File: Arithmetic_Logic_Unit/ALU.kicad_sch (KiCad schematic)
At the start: 21 parts, among them U3 74LS86, U4 74LS86, U5 74LS283, U6 74LS283, U7 74LS245

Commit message: added flags
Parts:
- added U10: 74LS08, symbol 74xx:74LS08
- added U11: 74LS02, symbol 74xx:74LS02
- added U9: 74LS173, symbol 74xx:74LS173
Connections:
- net 5V: now also U10.14 (VCC), U11.14 (VCC), U9.16 (VCC)
- net GND: now also U10.12, U10.13, U10.7 (GND), U11.7 (GND), U9.1 (Oe1), U9.2 (Oe2), U9.8 (GND)
- net clock: now also U9.7 (Cp)
- net s0: now also U11.12
- net s1: now also U11.11
- net s2: now also U11.9
- net s3: now also U11.8
- net s4: now also U11.6
- net s5: now also U11.5
- net s6: now also U11.3
- net s7: now also U11.2
- net at U5.9 (C4): now also U9.14 (D0)
- new net: U10.4, U11.10
- new net: U10.5, U11.13
- new net: U10.10, U10.6
- new net: U10.1, U11.1
- new net: U10.2, U11.4
- new net: U10.3, U10.9
- new net: U10.8, U9.13 (D1)
- new net cf: U9.3 (Q0)
- new net clear: U9.15 (Mr)
- new net fi: U9.10 (E2), U9.9 (E1)
- new net zf: U9.4 (Q1)
- no-connect marks 0 -> 5

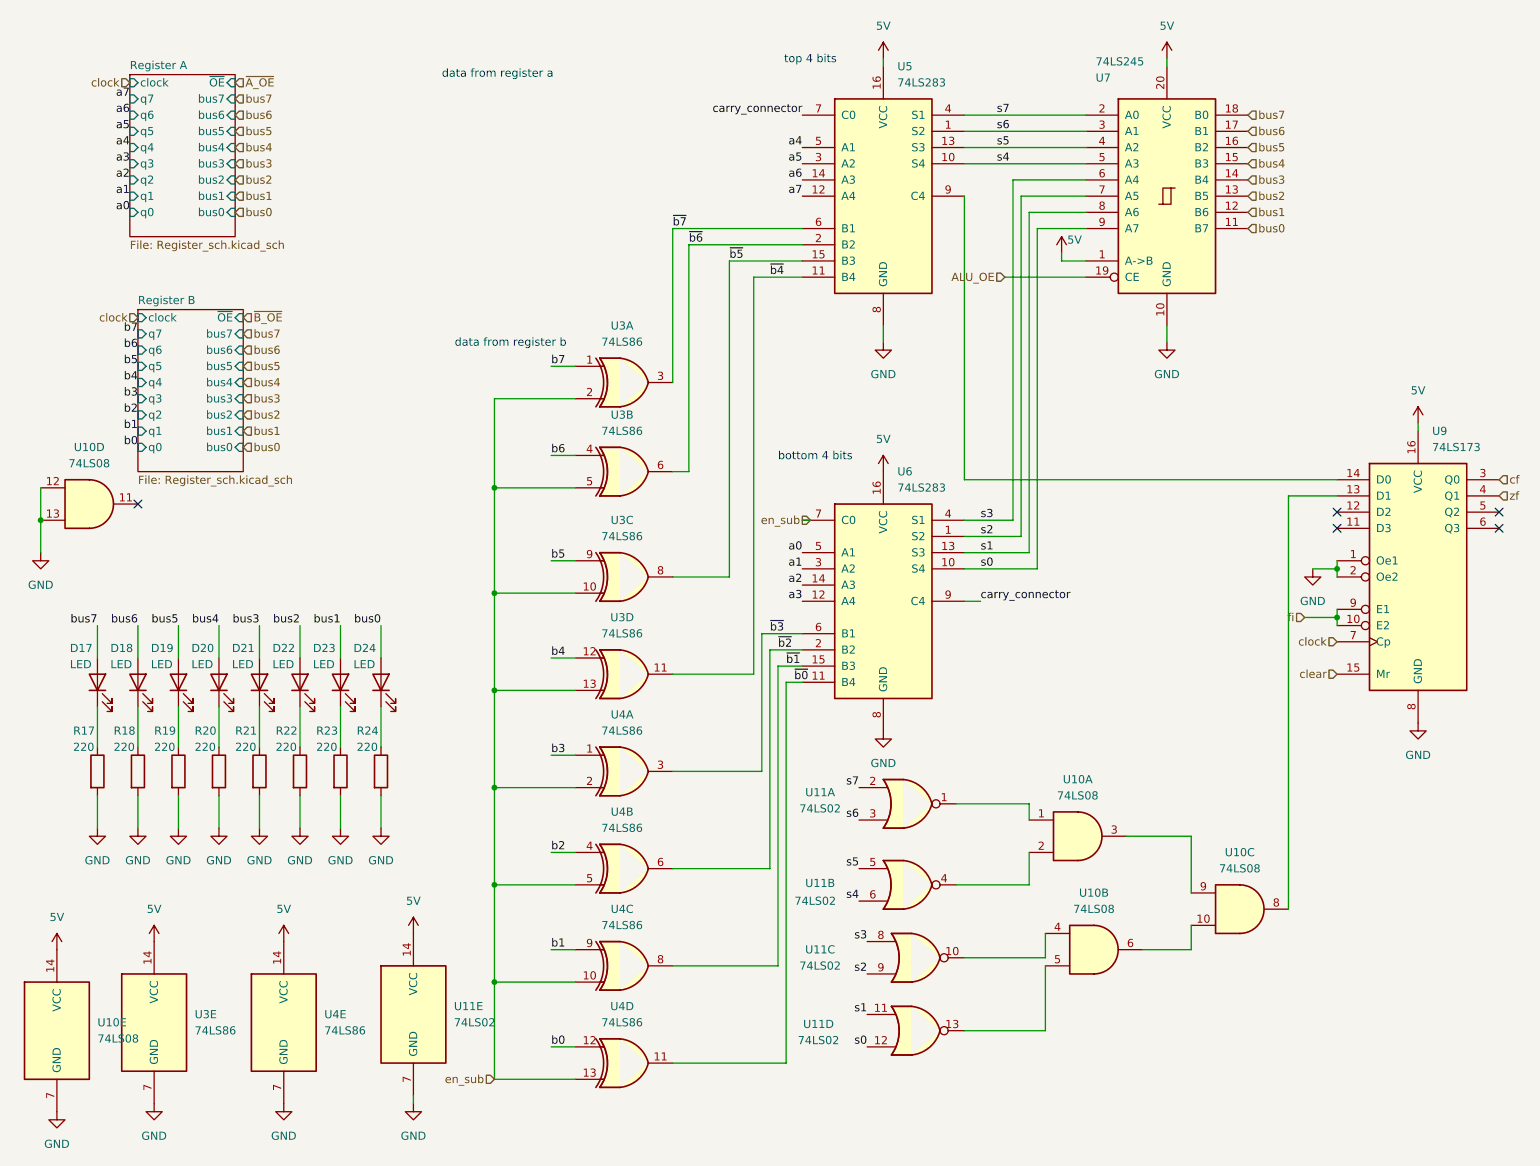
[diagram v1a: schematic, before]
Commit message: fixed incorrect footprint for sn54173
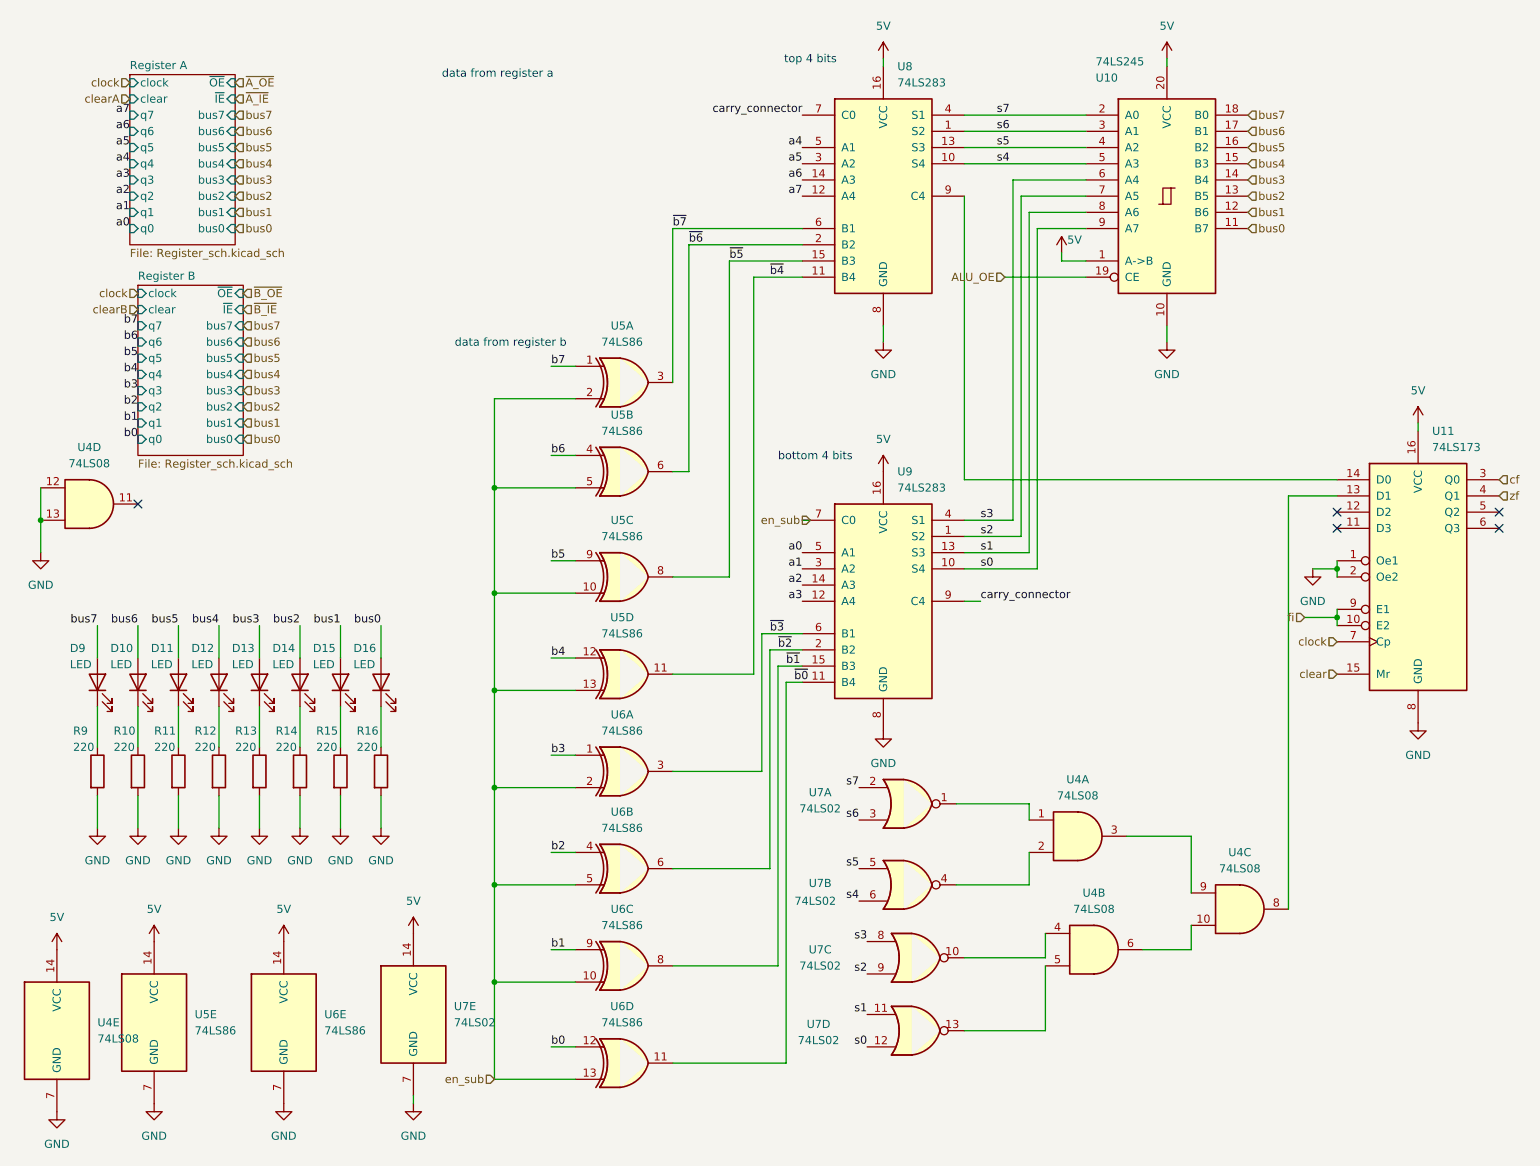
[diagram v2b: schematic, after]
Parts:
- renumbered D18 to D10, D19 to D11, D20 to D12, D21 to D13, D22 to D14, D23 to D15, D24 to D16, D17 to D9, R18 to R10, R19 to R11, R20 to R12, R21 to R13, R22 to R14, R23 to R15, R24 to R16, R17 to R9, U7 to U10, U9 to U11, U10 to U4, U3 to U5, U4 to U6, U11 to U7, U5 to U8, U6 to U9
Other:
- sheet Register A ports: added clear, ~{IE}; removed none
- sheet Register B ports: added clear, ~{IE}; removed none

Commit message: fixed wiring issues
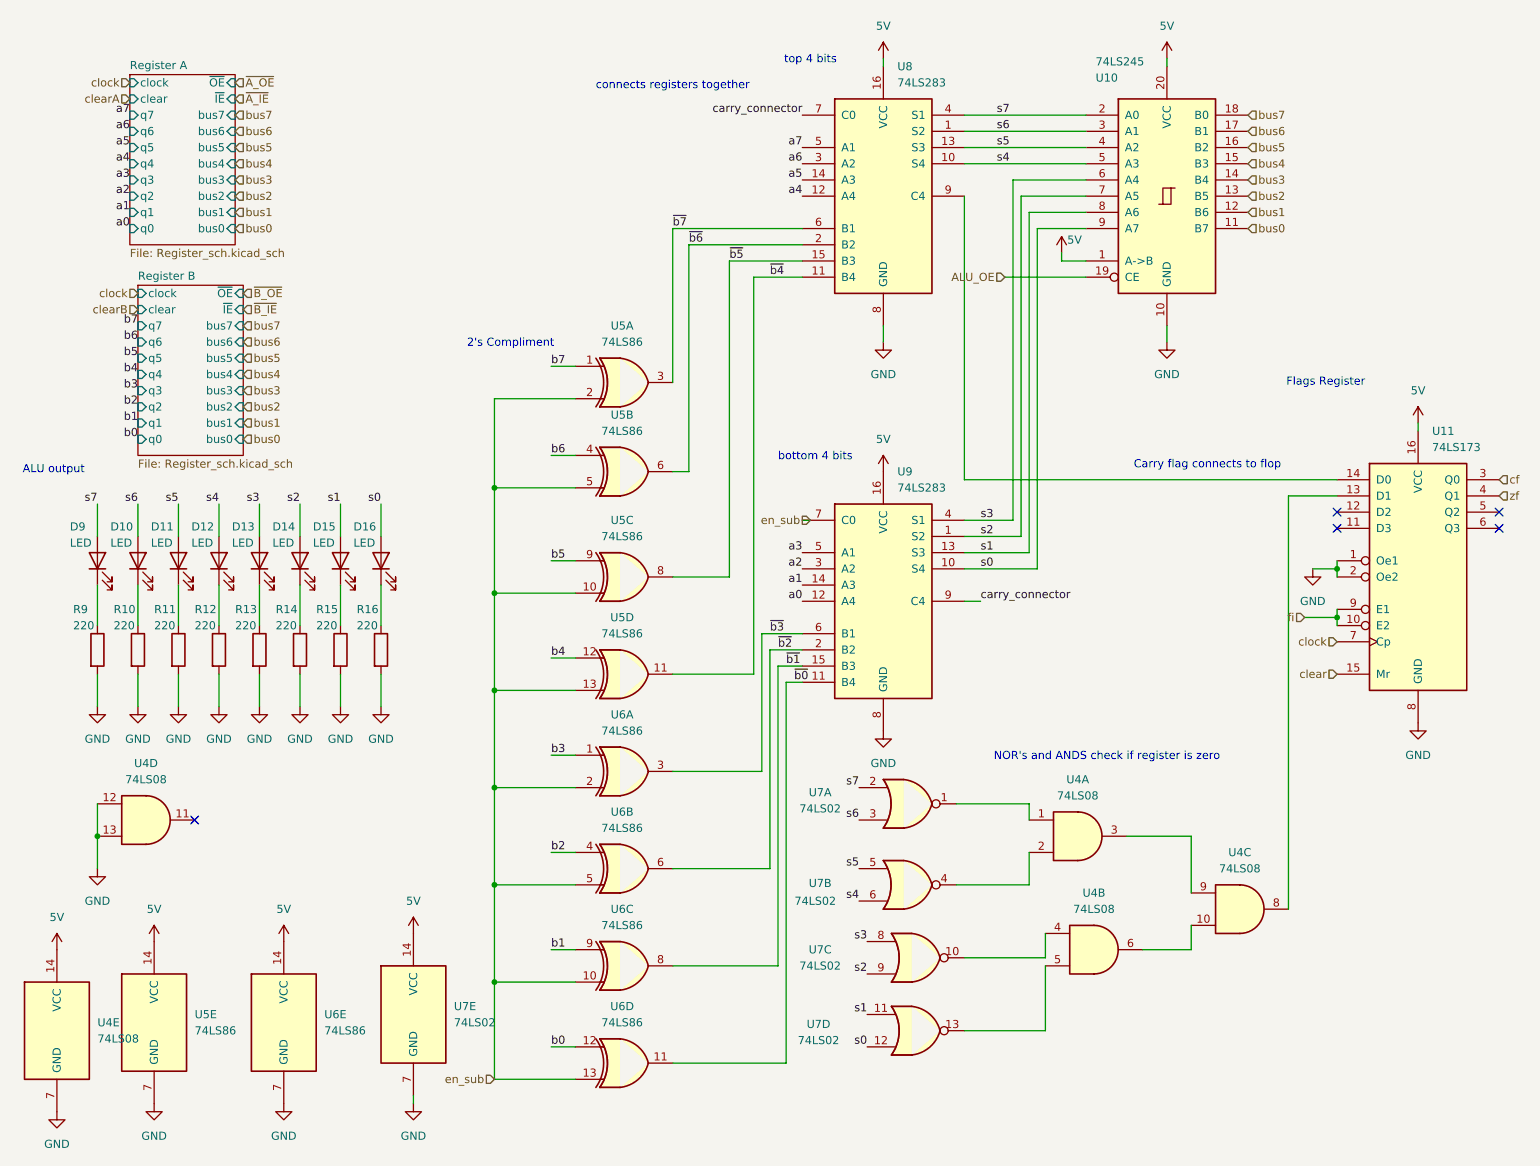
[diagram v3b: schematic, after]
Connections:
- net a0: now also U9.12 (A4); no longer U9.5 (A1)
- net a1: now also U9.14 (A3); no longer U9.3 (A2)
- net a2: now also U9.3 (A2); no longer U9.14 (A3)
- net a3: now also U9.5 (A1); no longer U9.12 (A4)
- net a4: now also U8.12 (A4); no longer U8.5 (A1)
- net a5: now also U8.14 (A3); no longer U8.3 (A2)
- net a6: now also U8.3 (A2); no longer U8.14 (A3)
- net a7: now also U8.5 (A1); no longer U8.12 (A4)
- net bus0: no longer D16.2 (A)
- net bus1: no longer D15.2 (A)
- net bus2: no longer D14.2 (A)
- net bus3: no longer D13.2 (A)
- net bus4: no longer D12.2 (A)
- net bus5: no longer D11.2 (A)
- net bus6: no longer D10.2 (A)
- net bus7: no longer D9.2 (A)
- net s0: now also D16.2 (A)
- net s1: now also D15.2 (A)
- net s2: now also D14.2 (A)
- net s3: now also D13.2 (A)
- net s4: now also D12.2 (A)
- net s5: now also D11.2 (A)
- net s6: now also D10.2 (A)
- net s7: now also D9.2 (A)
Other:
- note added: "2's Compliment"
- note added: "ALU output"
- note added: "Carry flag connects to flop"
- note added: "Flags Register"
- note added: "NOR's and ANDS check if register is zero"
- note added: "connects registers together"
- note removed: "data from register a"
- note removed: "data from register b"
- moved on the sheet: D10, D11, D12, D13, D14, D15, D16, D9, R10, R11, R12, R13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

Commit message: added bypass capacitors
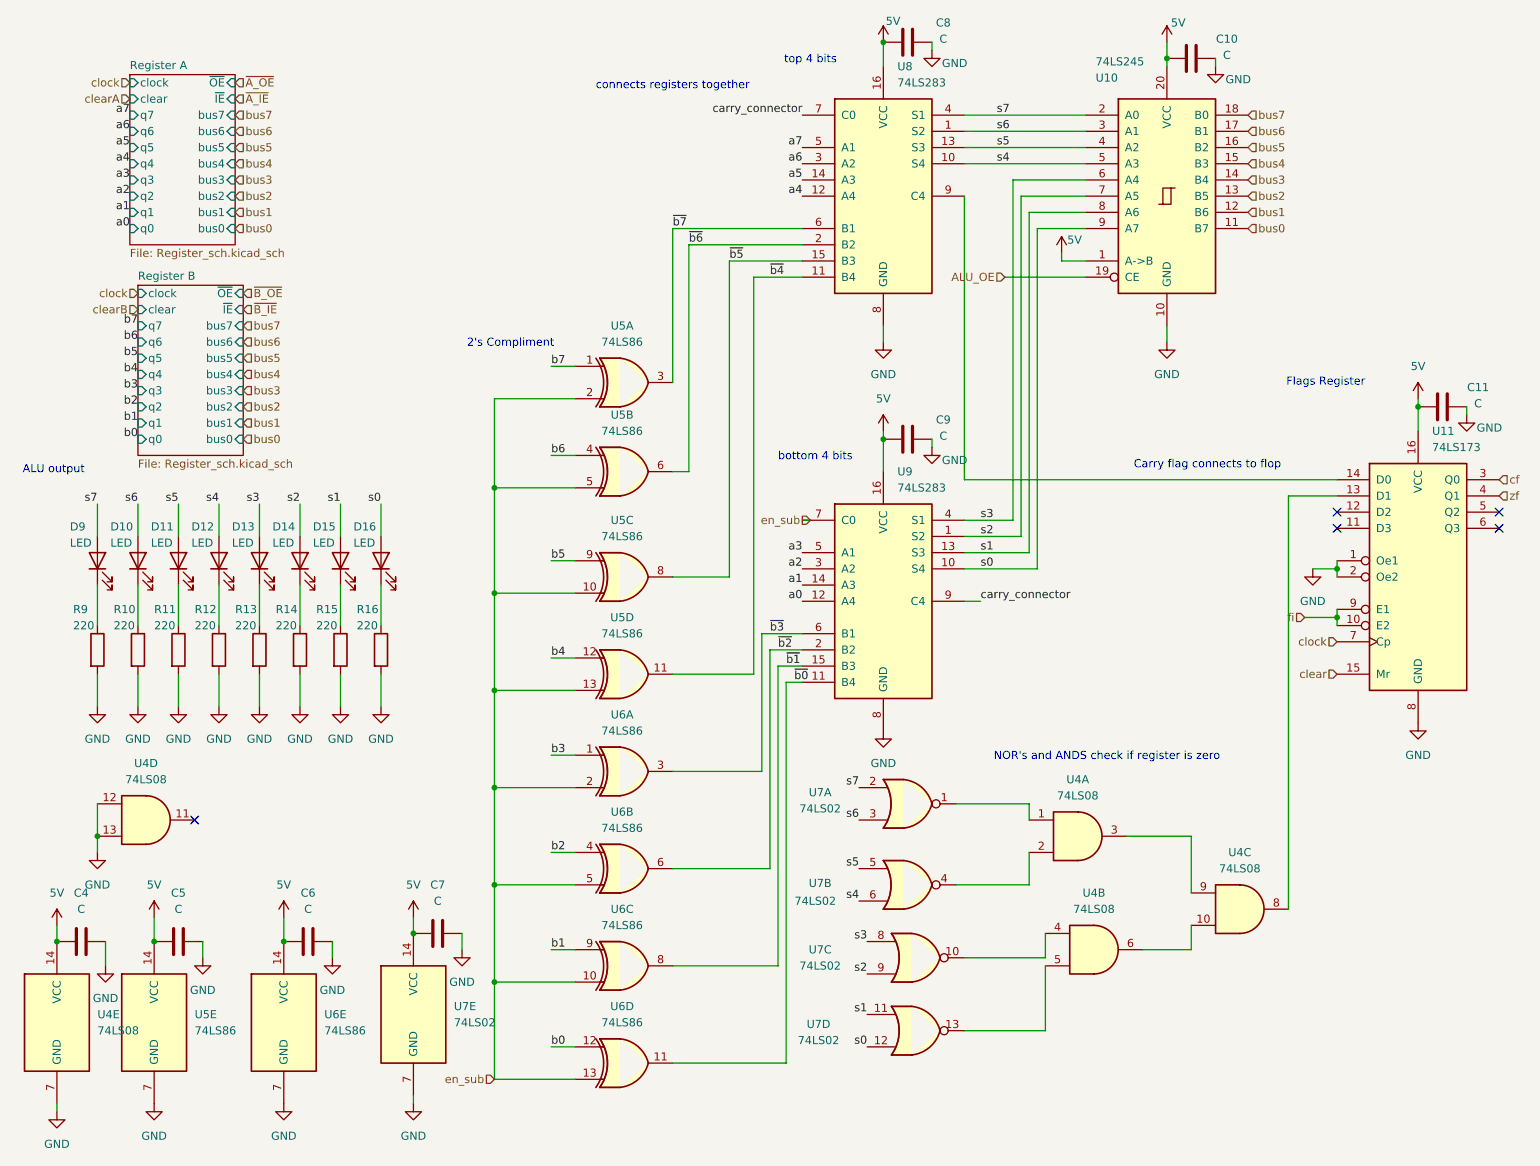
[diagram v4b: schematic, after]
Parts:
- added C10, C11, C4, C5, C6, C7, C8, C9: C, symbol Device:C
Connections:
- net 5V: now also C10.2, C11.2, C4.2, C5.2, C6.2, C7.2, C8.2, C9.2
- net GND: now also C10.1, C11.1, C4.1, C5.1, C6.1, C7.1, C8.1, C9.1
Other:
- moved on the sheet: U4E
